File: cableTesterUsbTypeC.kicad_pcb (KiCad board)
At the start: 2 copper layers, 30.6 x 29 mm, 53 parts, among them J1 USB_C_Receptacle, J3 USB_C_Receptacle

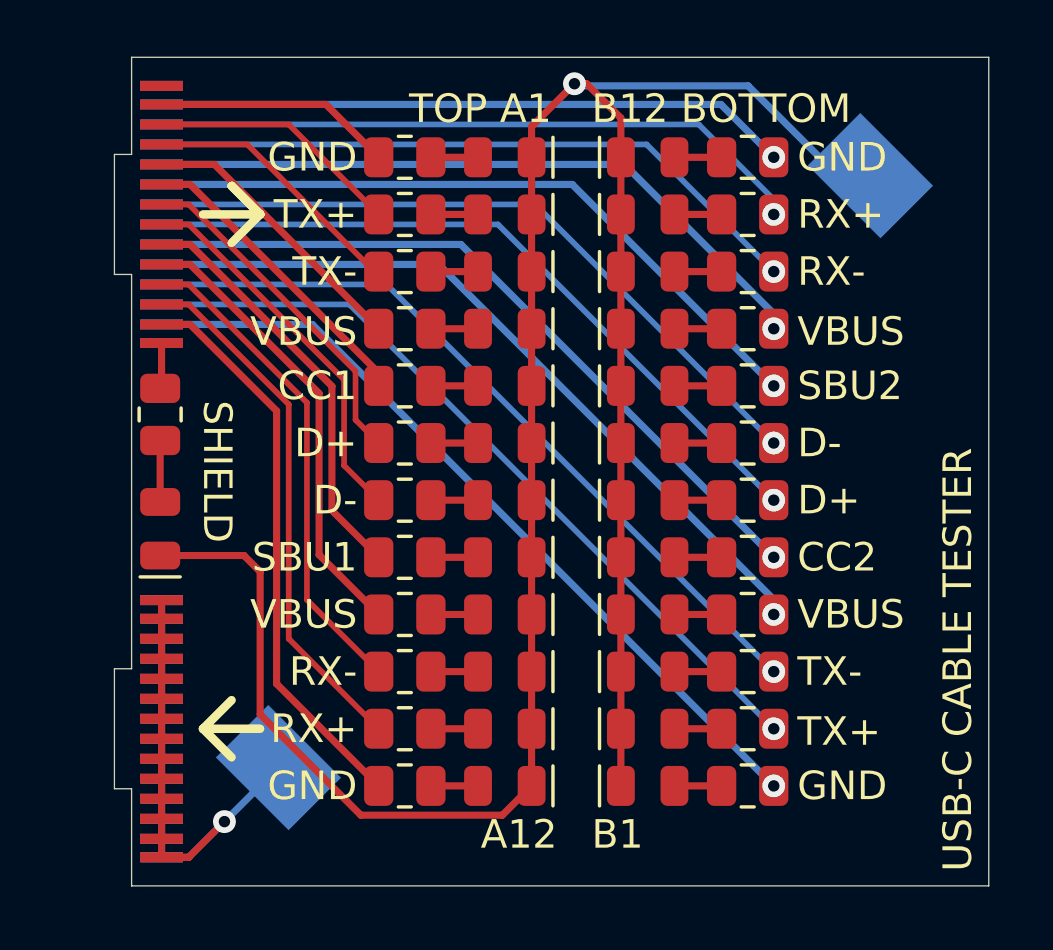
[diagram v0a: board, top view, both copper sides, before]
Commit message: Move indicators 2mm right, making room for protocol group labels
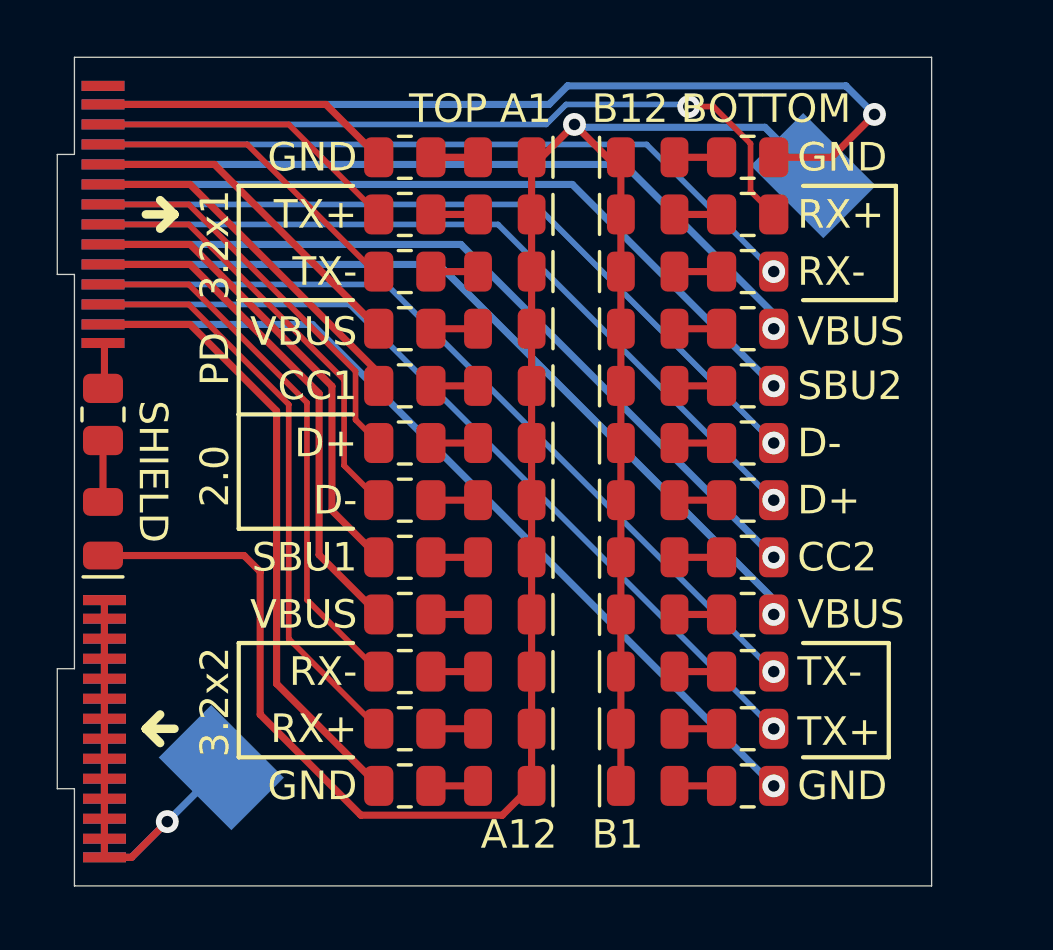
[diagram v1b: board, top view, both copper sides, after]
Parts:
- moved J3 2.05 mm to (27.5, 30.5)
- moved BT1 2.00 mm to (42.0, 39.5)
- moved D25 2.00 mm to (27.5, 41.5)
- moved J1 2.00 mm to (27.6, 48.5)
- moved R25 2.00 mm to (27.5, 37.5)
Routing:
- net /GND_B12: track 22.2 -> 31.8 mm
- net GND: track 82.5 -> 78.8 mm
- net /RX1+: track 23.0 -> 26.3 mm
- net /VBUS_B9: track 24.1 -> 26.1 mm
- net /VBUS_B4: track 26.8 -> 28.8 mm
- net /VBUS_A9: track 16.0 -> 18.0 mm
- net /VBUS_A4: track 9.98 -> 12.0 mm
- net /TX2-: track 27.0 -> 29.0 mm
- net /TX2+: track 27.6 -> 29.6 mm
- net /TX1-: track 9.44 -> 11.4 mm
- net /TX1+: track 8.90 -> 10.9 mm
- net /SBU2: track 24.3 -> 26.3 mm
- net /SBU1: track 14.7 -> 16.7 mm
- net /RX2-: track 17.3 -> 19.3 mm
- net /RX2+: track 18.6 -> 20.6 mm
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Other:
- board text added: "2.0"
- board text added: "3.2x1"
- board text added: "3.2x2"
- board text added: "PD"
- board text added: "USB-C Cable Tester"
- board text removed: "USB-C CABLE TESTER"

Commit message: Add QR/DataMatrix codes to wikipedia page with pin usage tables
https://en.wikipedia.org/w/index.php?title=USB-C&oldid=1169872296#USB-C
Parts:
- added G***: LOGO, Library:usbc_pin_url_datamatrix, B.Cu at (31.8, 28.5)
- added G***: LOGO, Library:usbc_pin_url_qr, B.Cu at (52.2, 49.8)
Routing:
- net /TX2-: track 29.0 -> 40.6 mm
- net /TX2+: track 29.6 -> 38.3 mm
- net /GND_B1: track 30.1 -> 37.7 mm
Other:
- board text added: "Cable Tester"
- board text added: "USB-C"
- board text removed: "USB-C Cable Tester"
